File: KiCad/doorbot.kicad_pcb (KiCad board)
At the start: 2 copper layers, 54 parts, among them J1 SERVO, J10 Raspberry_Pi_2_3, J2 POWER, J3 SIEDLE LED, J4 SIEDLE KEY, J5 ERT SWITCH, J6 ERT SIEDLE, J7 BUZZER, J8 UI LED, J9 UI BUTTON, Q1 BC337, Q2 BC548, Q3 BC548, U1 PC817, U2 PC817, U3 74HC14, U4 EPR211A064, U5 EPR211A064, U6 L4940, U7 MIC29302WT

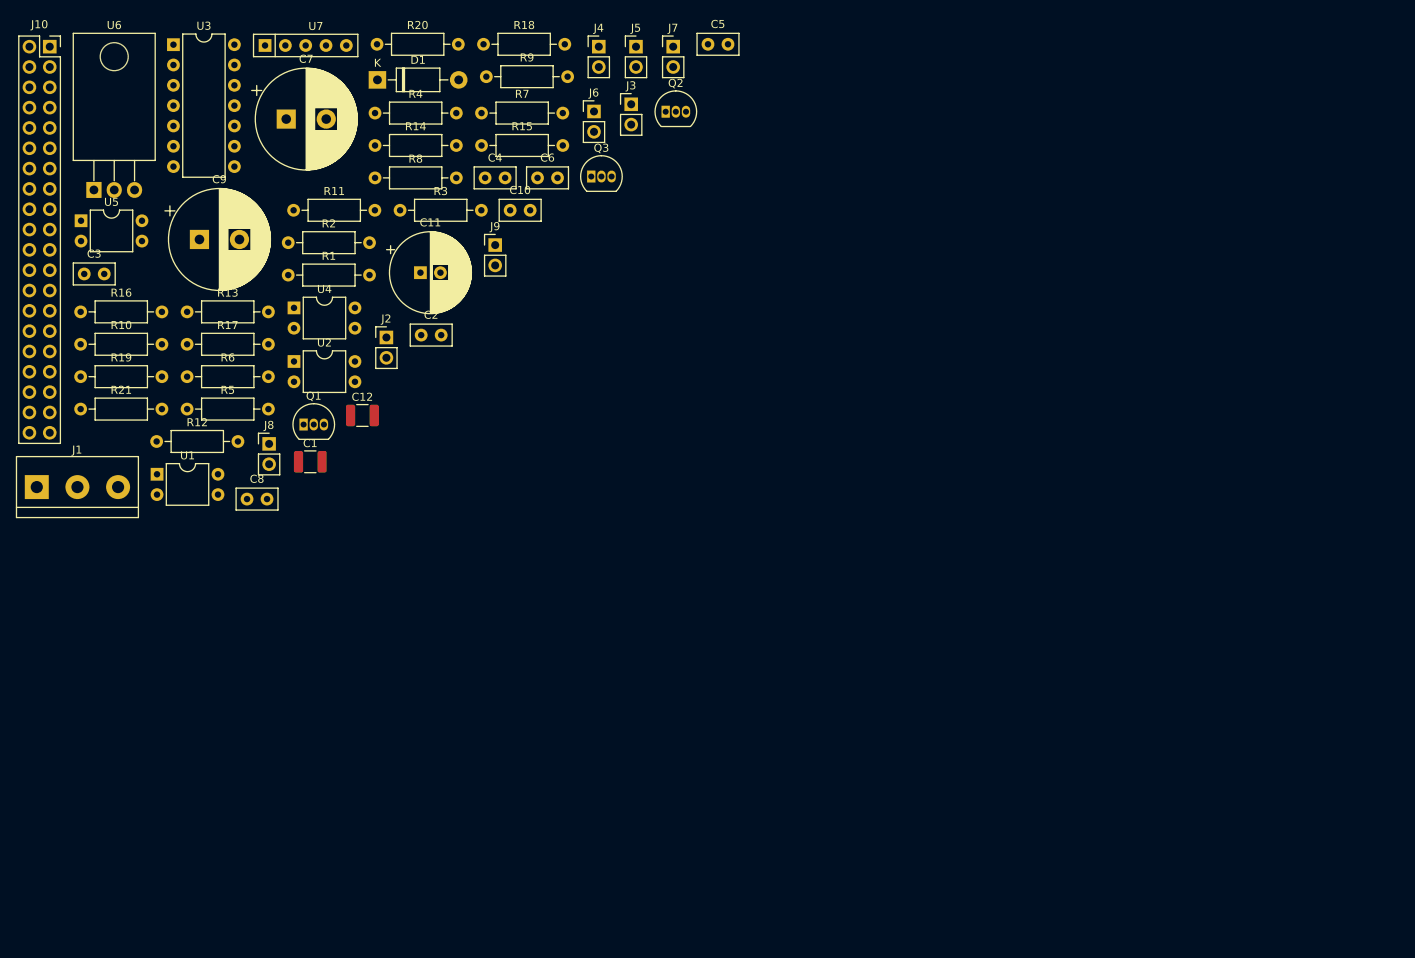
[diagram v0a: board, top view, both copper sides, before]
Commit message: Route the stripboard PCB
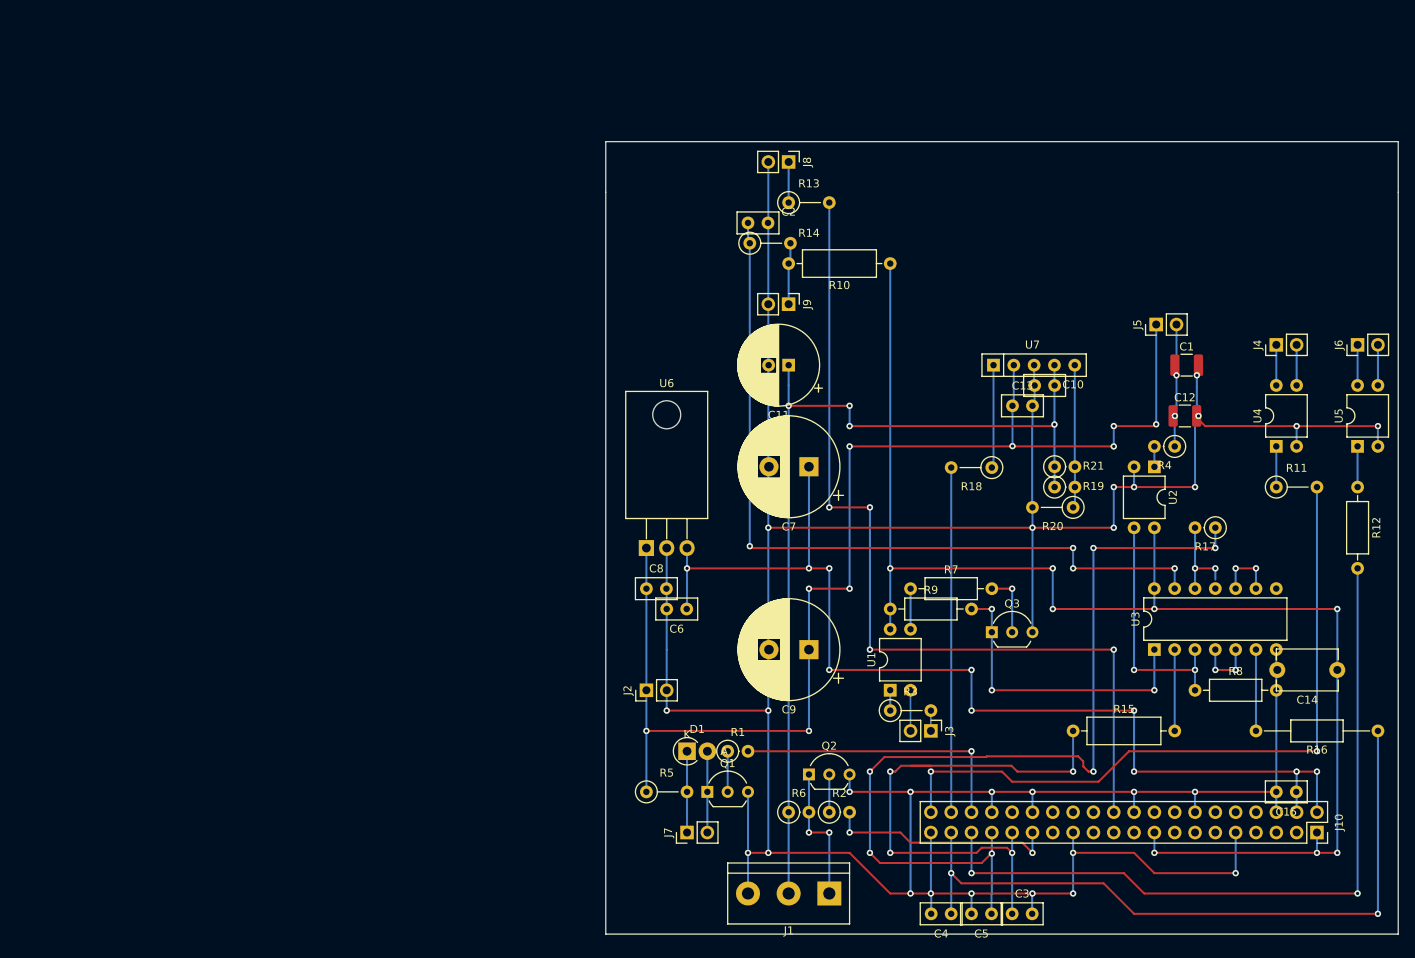
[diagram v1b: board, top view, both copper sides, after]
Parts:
- added C13: 100n, Capacitor_THT:C_Disc_D5.0mm_W2.5mm_P2.50mm, F.Cu at (190.5, 94.0)
- added C14: 100n, Capacitor_THT:C_Disc_D7.5mm_W5.0mm_P7.50mm, F.Cu at (231.1, 127.0)
- added C15: 100n, Capacitor_THT:C_Disc_D5.0mm_W2.5mm_P2.50mm, F.Cu at (226.0, 142.2)
- D1: footprint Diode_THT:D_DO-41_SOD81_P10.16mm_Horizontal -> Diode_THT:D_DO-41_SOD81_P2.54mm_Vertical_AnodeUp
- Q1, Q2, Q3: footprint Package_TO_SOT_THT:TO-92_Inline -> Package_TO_SOT_THT:TO-92_Inline_Wide
- R1, R17, R19, R2, R21, R4, R6: footprint Resistor_THT:R_Axial_DIN0207_L6.3mm_D2.5mm_P10.16mm_Horizontal -> Resistor_THT:R_Axial_DIN0207_L6.3mm_D2.5mm_P2.54mm_Vertical
- R10, R15: footprint Resistor_THT:R_Axial_DIN0207_L6.3mm_D2.5mm_P10.16mm_Horizontal -> Resistor_THT:R_Axial_DIN0309_L9.0mm_D3.2mm_P12.70mm_Horizontal
- R11, R13, R14, R18, R20, R3, R5: footprint Resistor_THT:R_Axial_DIN0207_L6.3mm_D2.5mm_P10.16mm_Horizontal -> Resistor_THT:R_Axial_DIN0207_L6.3mm_D2.5mm_P5.08mm_Vertical
- R16: footprint Resistor_THT:R_Axial_DIN0207_L6.3mm_D2.5mm_P10.16mm_Horizontal -> Resistor_THT:R_Axial_DIN0207_L6.3mm_D2.5mm_P15.24mm_Horizontal
- moved J10 186.4 mm to (228.6, 147.3), turned to -90 degrees
- moved R16 170.4 mm to (236.2, 134.6), turned to 180 degrees
- moved U5 162.0 mm to (233.7, 99.0), turned to 90 degrees
- moved R12 150.2 mm to (233.7, 104.1), turned to -90 degrees
- moved U3 144.1 mm to (208.3, 124.5), turned to 90 degrees
- moved C3 140.9 mm to (190.5, 157.5)
- moved R17 130.6 mm to (215.9, 109.2), turned to 180 degrees
- moved R11 127.6 mm to (223.5, 104.1)
- moved U4 124.0 mm to (223.5, 99.0), turned to 90 degrees
- moved R19 122.5 mm to (195.8, 104.1)
- moved R21 122.0 mm to (195.8, 101.6)
- moved R8 120.9 mm to (213.4, 129.5)
- moved C5 114.3 mm to (187.9, 157.5), turned to 180 degrees
- moved J1 111.3 mm to (167.6, 154.9), turned to 180 degrees
- moved C1 110.2 mm to (212.3, 88.9)
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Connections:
- U3 pad 10: (no net) -> Net-(U3-Pad10)
- U3 pad 11: (no net) -> unconnected-(U3-Pad11)
- U3 pad 12: (no net) -> Net-(R17-Pad2)
- U3 pad 13: (no net) -> Net-(C2-Pad1)
- U3 pad 8: Net-(R17-Pad2) -> unconnected-(U3-Pad8)
- U3 pad 9: Net-(C2-Pad1) -> Net-(U3-Pad10)
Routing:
- net GND: track 0.00 -> 460.2 mm, vias 0 -> 28
- net +3V3: track 0.00 -> 175.2 mm, vias 0 -> 8
- net +7.5V: track 0.00 -> 155.1 mm, vias 0 -> 9
- net +5V: track 0.00 -> 134.6 mm, vias 0 -> 10
- net +6V: track 0.00 -> 117.2 mm, vias 0 -> 4
- net /pi_ui_button_input: track 0.00 -> 112.3 mm, vias 0 -> 6
- net /pi_ui_led: track 0.00 -> 111.8 mm, vias 0 -> 4
- net Net-(C2-Pad1): track 0.00 -> 99.0 mm, vias 0 -> 4
- net /pi_ert_out: track 0.00 -> 95.0 mm, vias 0 -> 2
- net /pi_key_out: track 0.00 -> 88.5 mm, vias 0 -> 2
- net /pi_ert_input: track 0.00 -> 88.5 mm, vias 0 -> 2
- net /pi_led_input: track 0.00 -> 67.1 mm, vias 0 -> 4
- net /pi_6v_en: track 0.00 -> 43.1 mm
- net Net-(Q3-Pad1): track 0.00 -> 38.1 mm, vias 0 -> 3
- net /pi_buzzer: track 0.00 -> 35.6 mm, vias 0 -> 1
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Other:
- board outline added: 99.1 x 99.1 mm

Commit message: Add the final PCB version
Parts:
- added FB1: Bead, Resistor_THT:R_Axial_DIN0207_L6.3mm_D2.5mm_P10.16mm_Horizontal, F.Cu at (205.7, 139.7)
- C1: moved to B.Cu
- C11: value 100u -> 100n; footprint Capacitor_THT:CP_Radial_D10.0mm_P2.50mm -> Capacitor_THT:C_Disc_D5.0mm_W2.5mm_P2.50mm
- C12: value 22u -> 2200u 10V; footprint Capacitor_SMD:C_1210_3225Metric -> Capacitor_THT:CP_Radial_D12.5mm_P5.00mm
- C13: value 100n -> 1000u 16V; footprint Capacitor_THT:C_Disc_D5.0mm_W2.5mm_P2.50mm -> Capacitor_THT:CP_Radial_D12.5mm_P5.00mm
- C14: footprint Capacitor_THT:C_Disc_D7.5mm_W5.0mm_P7.50mm -> Capacitor_THT:C_Disc_D5.0mm_W2.5mm_P2.50mm
- C15: value 100n -> 100u; footprint Capacitor_THT:C_Disc_D5.0mm_W2.5mm_P2.50mm -> Capacitor_THT:CP_Radial_D10.0mm_P2.50mm
- C2: value 470n -> 22u; footprint Capacitor_THT:C_Disc_D5.0mm_W2.5mm_P2.50mm -> Capacitor_SMD:C_1210_3225Metric; moved to B.Cu
- C3: value 100n -> 470n
- C7: value 470u -> 100n; footprint Capacitor_THT:CP_Radial_D12.5mm_P5.00mm -> Capacitor_THT:C_Disc_D7.5mm_W5.0mm_P7.50mm
- C9: value 470u -> 100n; footprint Capacitor_THT:CP_Radial_D12.5mm_P5.00mm -> Capacitor_THT:C_Disc_D5.0mm_W2.5mm_P2.50mm
- R7, R9: footprint Resistor_THT:R_Axial_DIN0207_L6.3mm_D2.5mm_P10.16mm_Horizontal -> Resistor_THT:R_Axial_DIN0309_L9.0mm_D3.2mm_P12.70mm_Horizontal
- moved C3 92.5 mm to (157.5, 71.1)
- moved C15 82.9 mm to (162.6, 88.9)
- moved C7 70.8 mm to (231.1, 127.0)
- moved C10 59.1 mm to (226.1, 142.2)
- moved C2 59.0 mm to (211.9, 94.0)
- moved C6 53.9 mm to (188.0, 157.5)
- moved C14 50.3 mm to (195.6, 91.4)
- moved C12 47.4 mm to (165.1, 101.6), turned to 180 degrees
- moved C13 39.7 mm to (165.1, 124.5), turned to 180 degrees
- moved C11 28.4 mm to (190.5, 94.0), turned to 0 degrees
- moved C9 22.2 mm to (144.8, 115.6), turned to 0 degrees
- moved C4 7.62 mm to (190.5, 157.5), turned to 0 degrees
- moved C8 5.64 mm to (149.8, 119.4), turned to 180 degrees
- moved C5 5.04 mm to (182.9, 157.5)
- moved C1 0.22 mm to (212.1, 88.9)
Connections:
- C10 pad 1: +6V -> Net-(J10-Pad2)
- C11 pad 1: +6V -> +7.5V
- C12 pad 1: /ert_switch_2 -> +5V
- C14 pad 1: +3V3 -> +6V
- C15 pad 1: +5V -> +6V
- C2 pad 1: Net-(C2-Pad1) -> /ert_switch_2
- C3 pad 1: /pi_led_input -> Net-(C3-Pad1)
- C4 pad 1: /pi_ert_input -> /pi_led_input
- C5 pad 1: /pi_ui_button_input -> /pi_ert_input
- C6 pad 1: +5V -> /pi_ui_button_input
- C7 pad 1: +5V -> +3V3
- C8 pad 1: +7.5V -> +5V
- J10 pad 2: +5V -> Net-(J10-Pad2)
- J10 pad 4: +5V -> Net-(J10-Pad2)
- R14 pad 1: Net-(C2-Pad1) -> Net-(C3-Pad1)
- U3 pad 13: Net-(C2-Pad1) -> Net-(C3-Pad1)
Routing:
- net Net-(C3-Pad1): track 0.00 -> 99.0 mm, vias 0 -> 4
- net Net-(C2-Pad1): track 99.0 -> 0.00 mm, vias 4 -> 0
- net +5V: track 134.6 -> 101.6 mm, vias 10 -> 7
- net Net-(J10-Pad2): track 0.00 -> 22.9 mm, vias 0 -> 3
- net GND: track 460.2 -> 479.5 mm, vias 28 -> 27
- net /pi_ert_out: track 95.0 -> 97.9 mm
- net Net-(Q3-Pad1): track 38.1 -> 35.6 mm, vias 3 -> 2
- net Net-(Q3-Pad2): track 7.98 -> 5.44 mm, vias 1 -> 0
- net /pi_ert_input: track 88.5 -> 89.5 mm
- net +3V3: track 175.2 -> 174.5 mm
- net /ert_switch_2: track 15.7 -> 15.5 mm, vias 2 -> 0
- net (no net): vias 0 -> 1
